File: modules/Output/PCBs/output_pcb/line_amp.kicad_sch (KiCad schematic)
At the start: 23 parts, among them U7 TL074, U8 NE5532, U9 NE5532

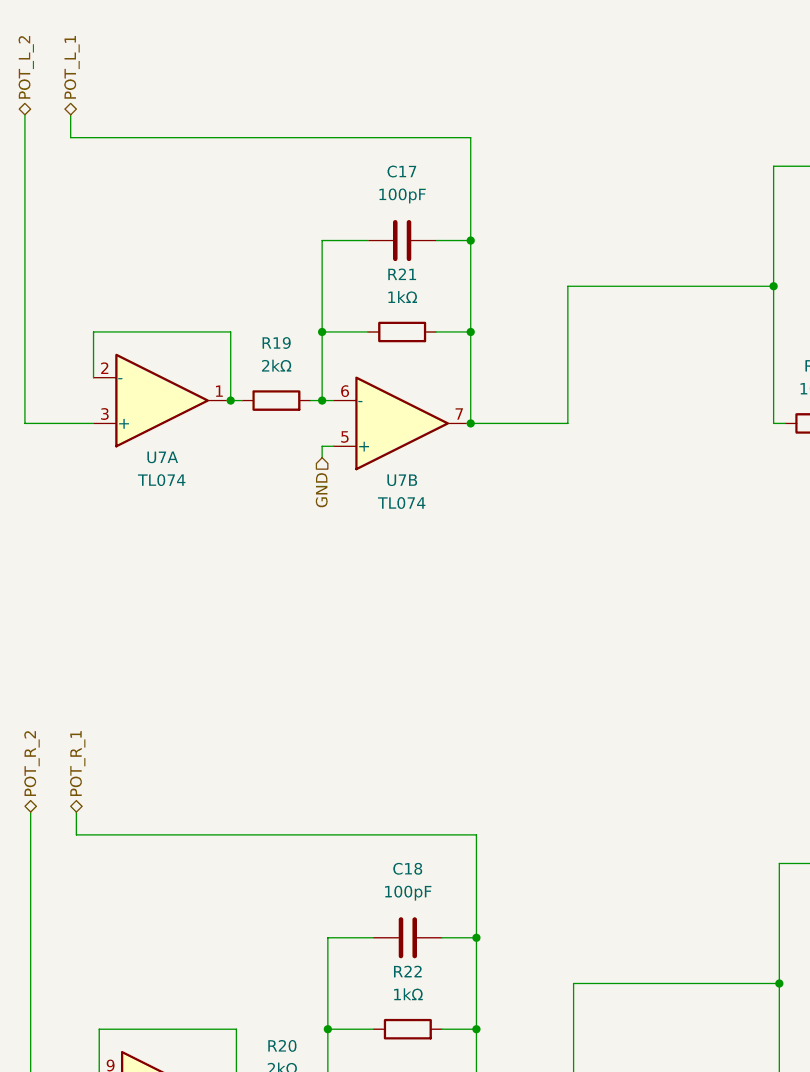
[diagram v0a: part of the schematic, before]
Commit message: finish output PCB
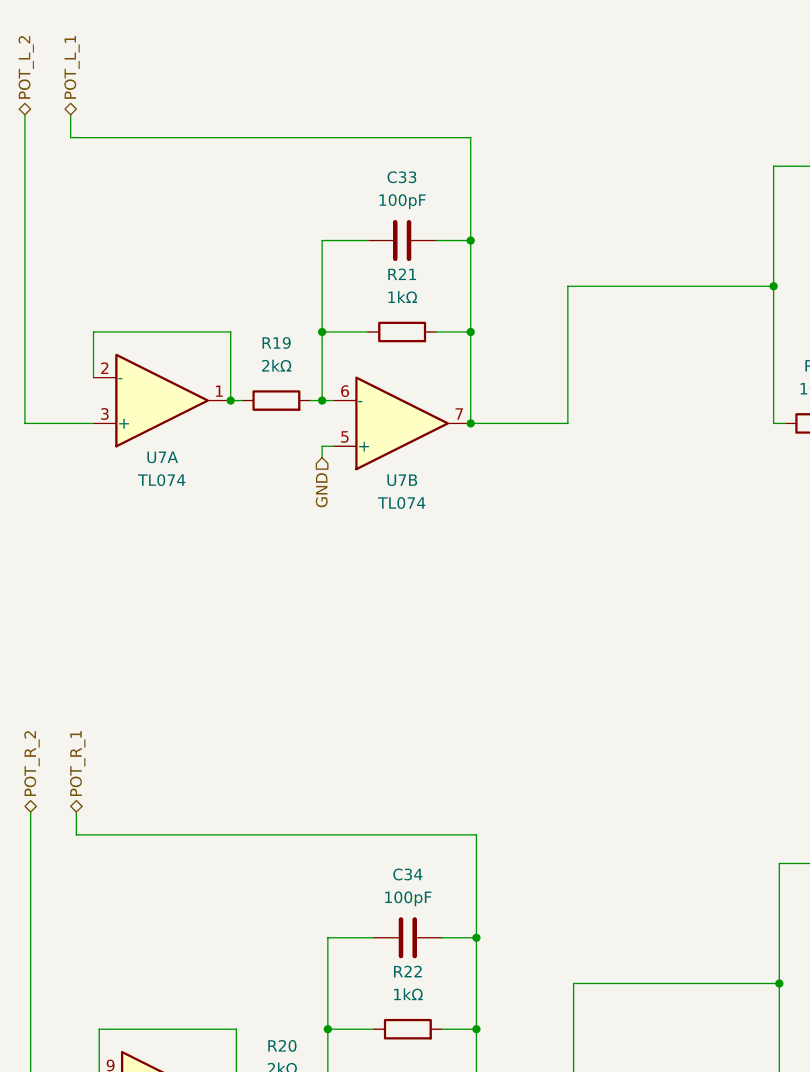
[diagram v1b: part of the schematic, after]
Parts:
- renumbered C17 to C33, C18 to C34
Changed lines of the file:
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@@
   (symbol (lib_id "Device:C") (at 88.265 125.095 90) (unit 1)
     (in_bom yes) (on_board yes) (dnp no) (fields_autoplaced)
-    (property "Reference" "C18" (at 88.265 117.475 90)
+    (property "Reference" "C34" (at 88.265 118.11 90)
       (effects (font (size 1.27 1.27)))
     )
-    (property "Value" "100pF" (at 88.265 120.015 90)
+    (property "Value" "100pF" (at 88.265 120.65 90)
       (effects (font (size 1.27 1.27)))
     )
@@
       (project "output_pcb"
         (path "/9afe4d4d-3155-44ea-9484-068db54e495a/1f69d69c-c7f1-4c71-9890-5c181d5a0d7a"
-          (reference "C18") (unit 1)
+          (reference "C34") (unit 1)
         )
       )
@@
   (symbol (lib_id "Device:C") (at 87.63 47.625 90) (unit 1)
     (in_bom yes) (on_board yes) (dnp no) (fields_autoplaced)
-    (property "Reference" "C17" (at 87.63 40.005 90)
+    (property "Reference" "C33" (at 87.63 40.64 90)
       (effects (font (size 1.27 1.27)))
     )
-    (property "Value" "100pF" (at 87.63 42.545 90)
+    (property "Value" "100pF" (at 87.63 43.18 90)
       (effects (font (size 1.27 1.27)))
     )
@@
       (project "output_pcb"
         (path "/9afe4d4d-3155-44ea-9484-068db54e495a/1f69d69c-c7f1-4c71-9890-5c181d5a0d7a"
-          (reference "C17") (unit 1)
+          (reference "C33") (unit 1)
         )
       )

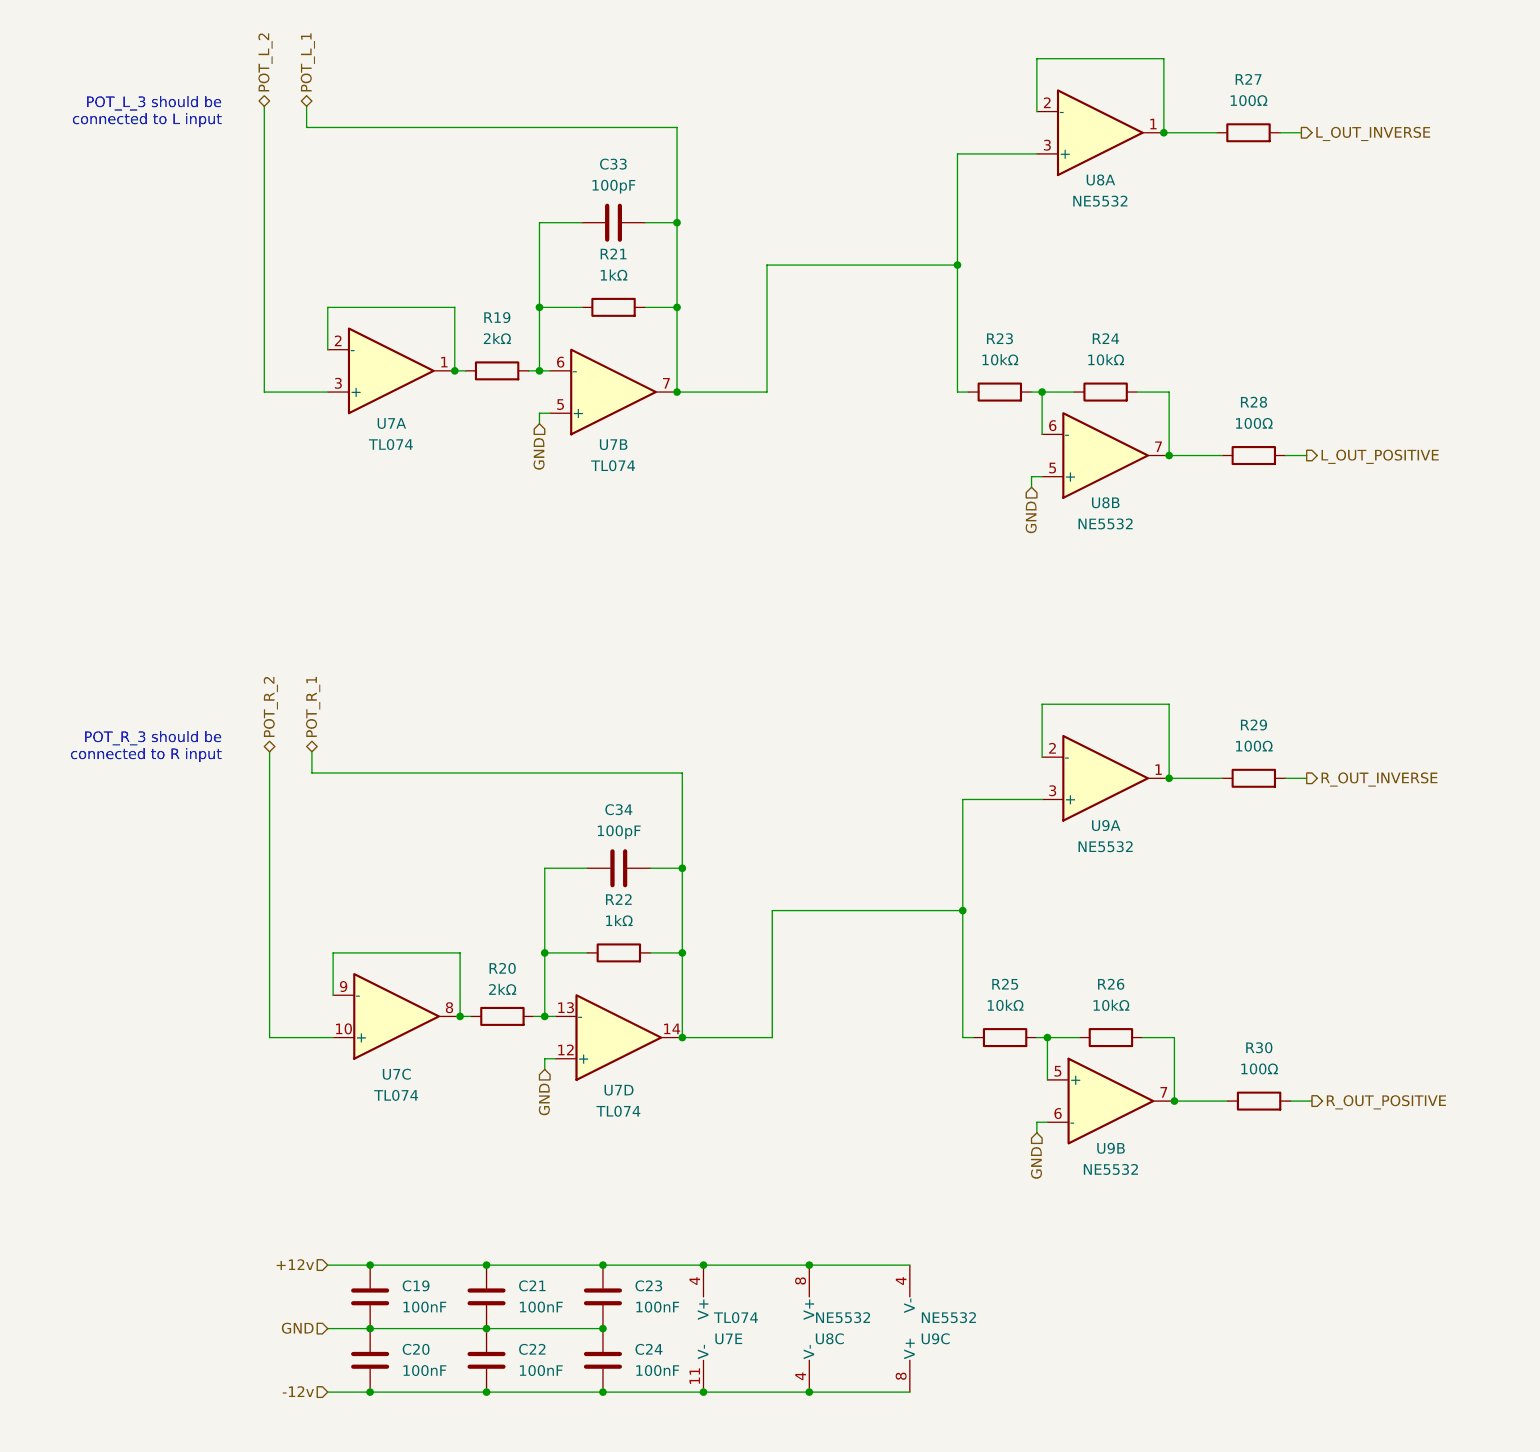
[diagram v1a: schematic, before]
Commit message: fix polarity mismatch bugs in output pcb
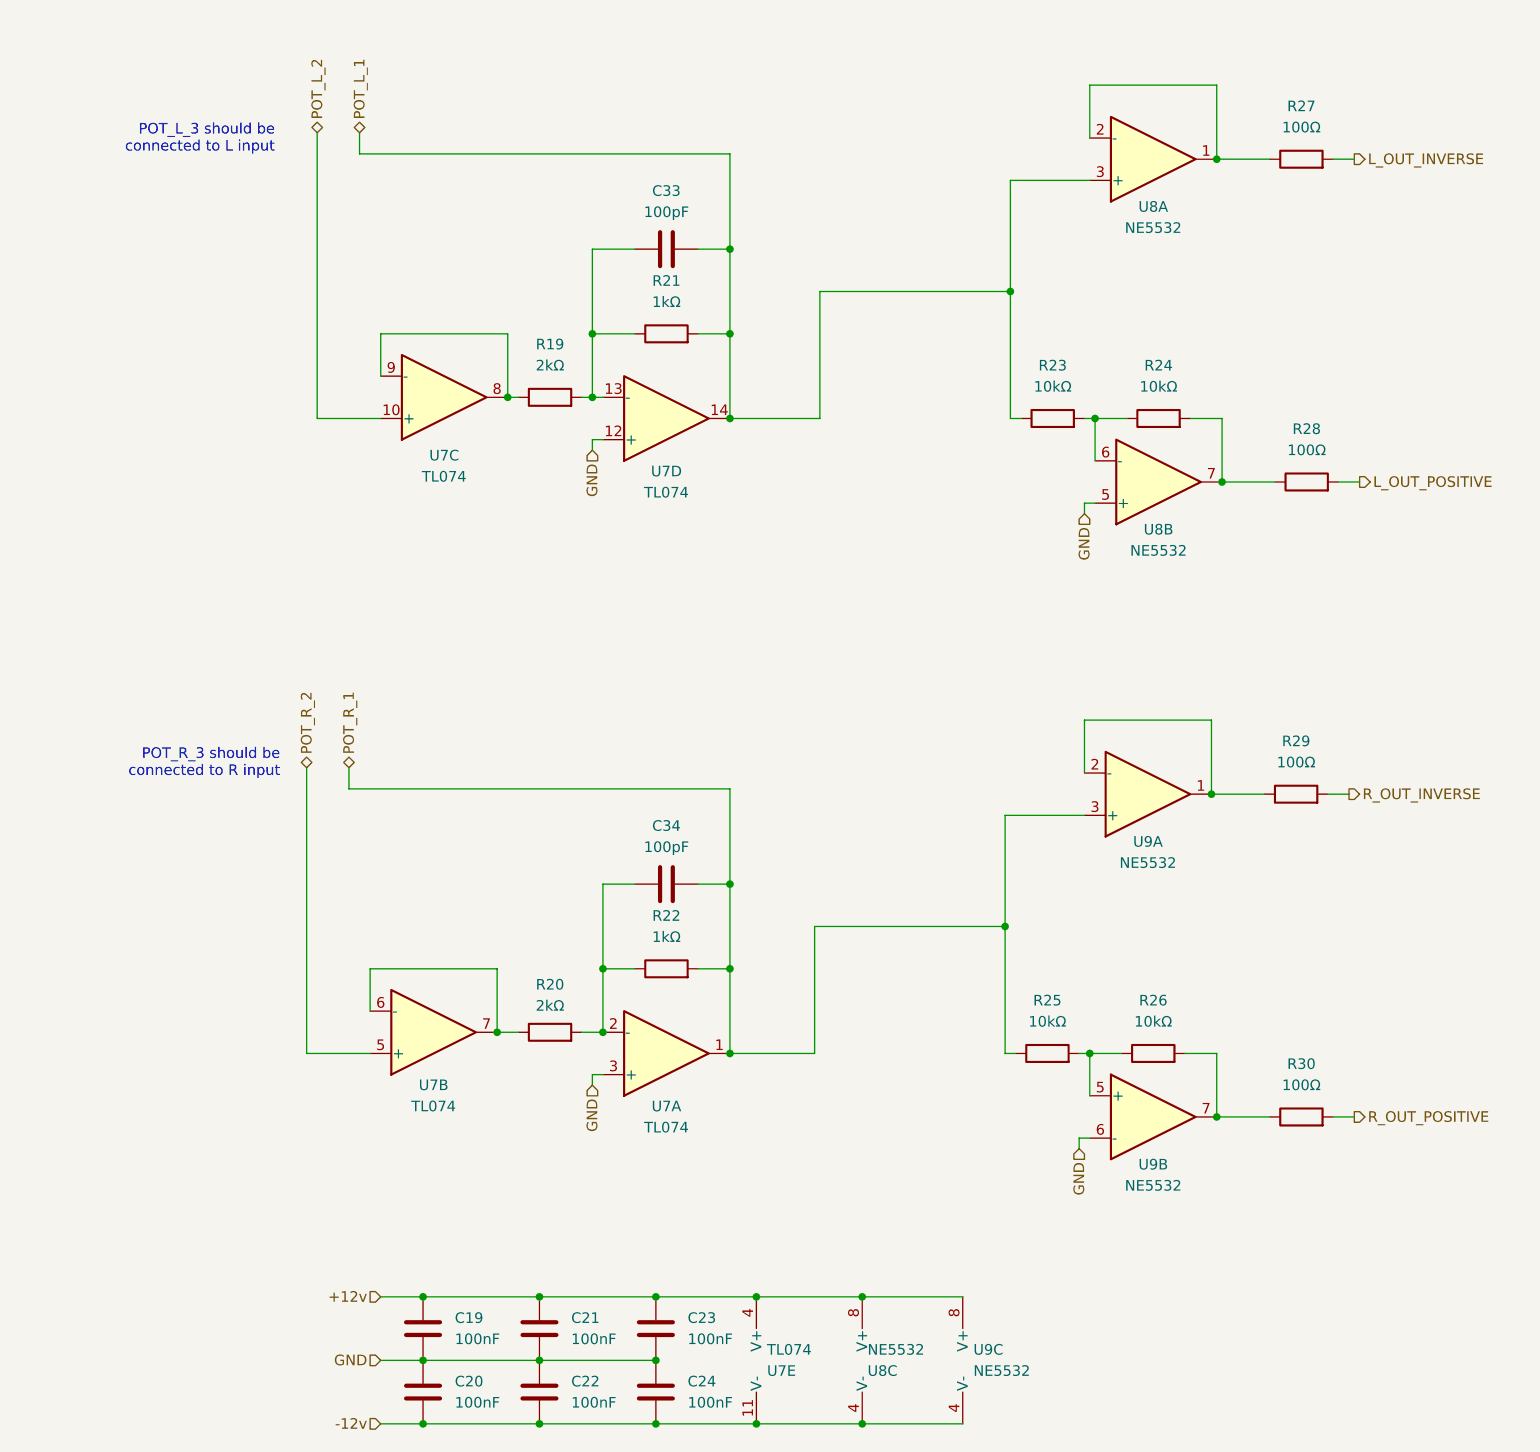
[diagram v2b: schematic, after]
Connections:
- net +12v: now also U9.8 (V+); no longer U9.4 (V-)
- net -12v: now also U9.4 (V-); no longer U9.8 (V+)
- net GND: now also U7.3 (+); no longer U7.5 (+)
- net POT_L_1: now also U7.14; no longer U7.7
- net POT_L_2: now also U7.10 (+); no longer U7.3 (+)
- net POT_R_1: now also U7.1; no longer U7.14
- net POT_R_2: now also U7.5 (+); no longer U7.10 (+)
- net at C34.1, R20.2, R22.1: now also U7.2 (-); no longer U7.13 (-)
- net at U7.8, U7.9 (-): now also R19.1; no longer R20.1
- net at C33.1, R19.2, R21.1: now also U7.13 (-); no longer U7.6 (-)
- new net: R20.1, U7.6 (-), U7.7
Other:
- company: (none) -> Free Modular
- title: (none) -> Output
- moved on the sheet: C19, C20, C21, C22, C23, C24, C33, C34, R19, R20, R21, R22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

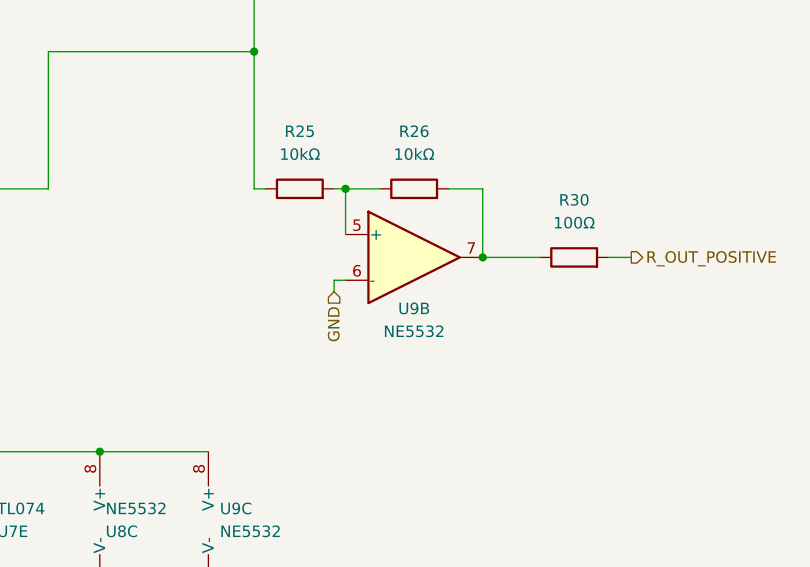
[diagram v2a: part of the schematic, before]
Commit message: Fix errors in output PCB
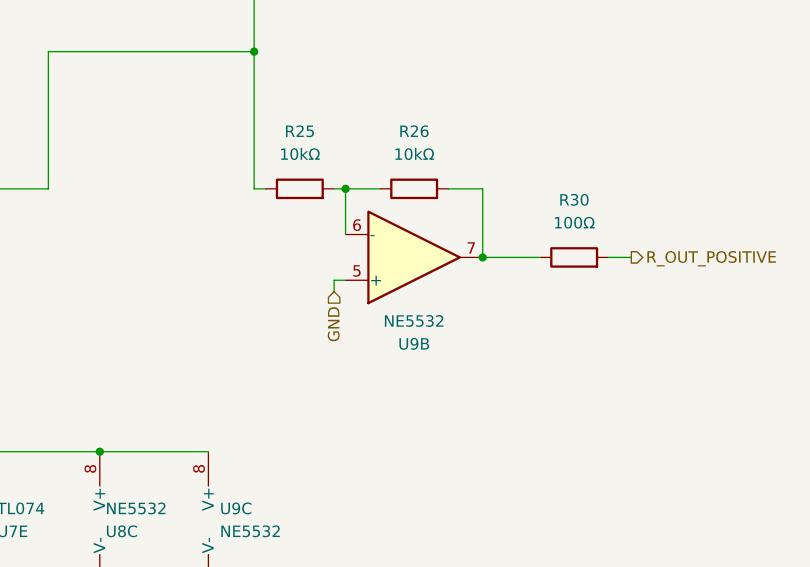
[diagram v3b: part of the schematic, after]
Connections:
- net GND: now also U9.5 (+); no longer U9.6 (-)
- net at R25.2, R26.1: now also U9.6 (-); no longer U9.5 (+)
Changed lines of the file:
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@@
 		(lib_id "Amplifier_Operational:NE5532")
 		(at 152.4 154.94 0)
+		(mirror x)
 		(unit 2)
 		(exclude_from_sim no)
@@
 		(dnp no)
 		(property "Reference" "U9"
-			(at 152.4 160.655 0)
+			(at 152.4 164.592 0)
 			(effects
 				(font
@@
 		)
 		(property "Value" "NE5532"
-			(at 152.4 163.195 0)
+			(at 152.4 162.052 0)
 			(effects
 				(font

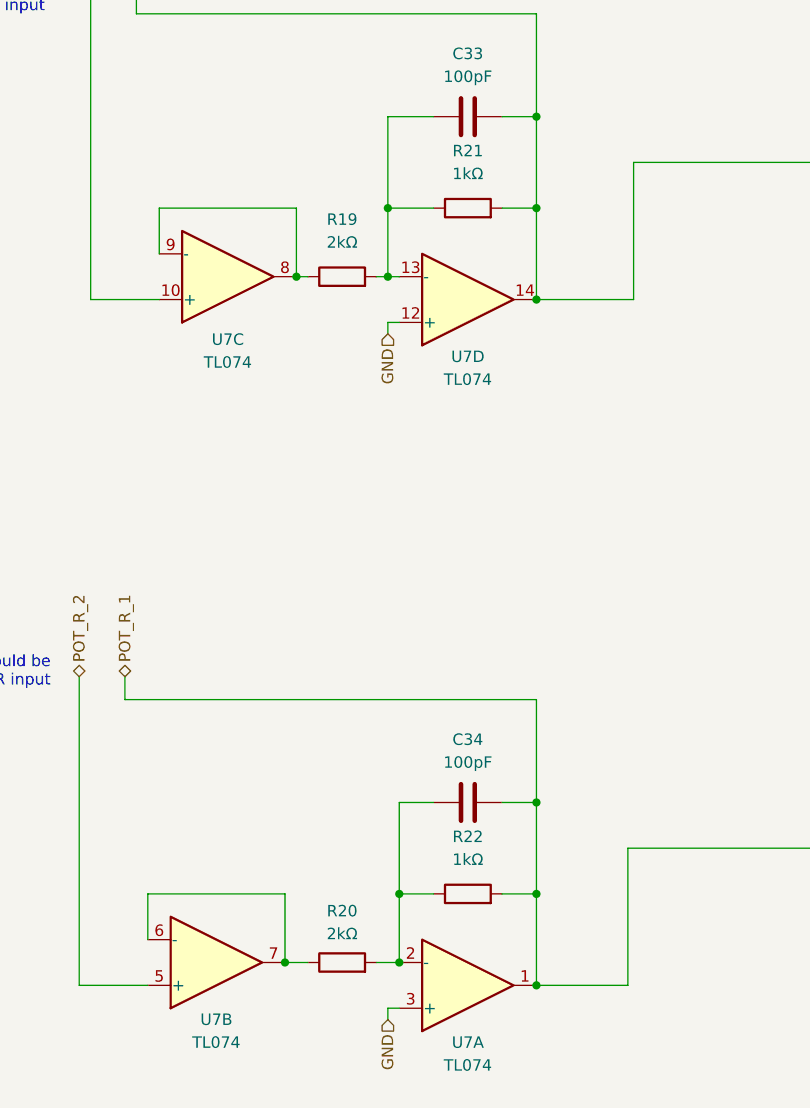
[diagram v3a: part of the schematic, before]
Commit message: Update resistor values in output amp
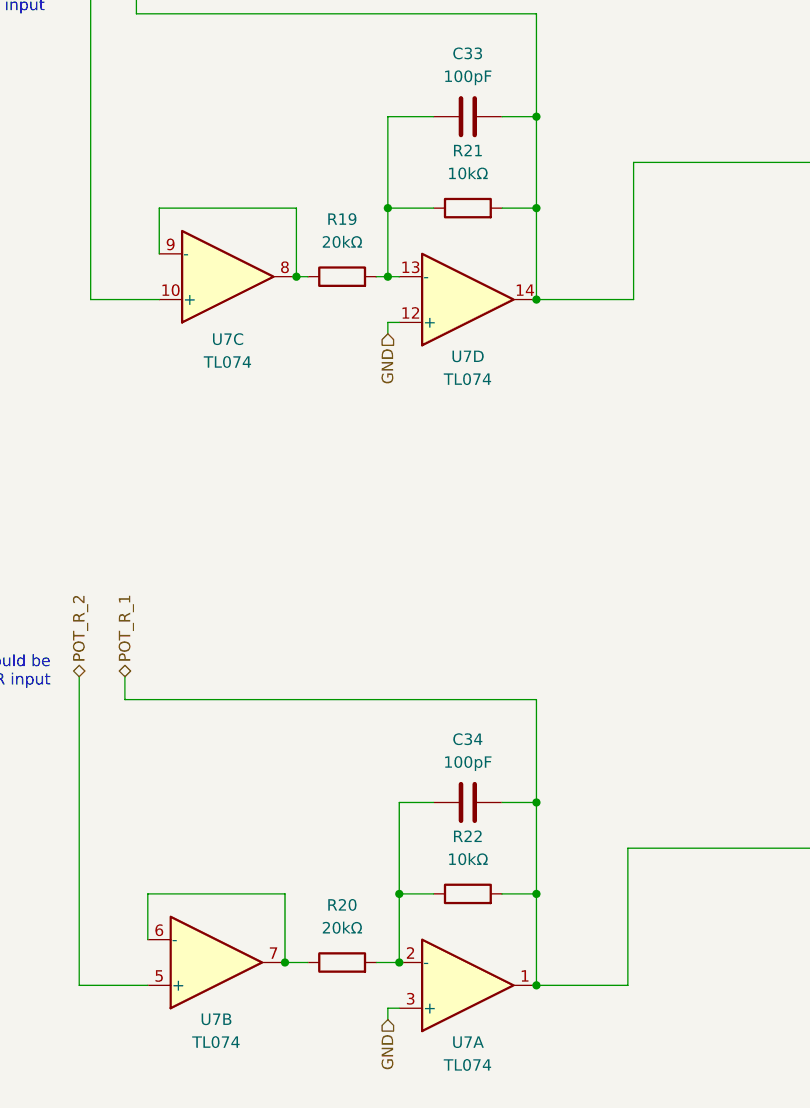
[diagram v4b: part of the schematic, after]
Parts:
- R19, R20: value 2kΩ -> 20kΩ
- R21, R22: value 1kΩ -> 10kΩ
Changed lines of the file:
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@@
 			)
 		)
-		(property "Value" "1kΩ"
+		(property "Value" "10kΩ"
 			(at 93.98 133.35 90)
 			(effects
@@
 			)
 		)
-		(property "Value" "2kΩ"
+		(property "Value" "20kΩ"
 			(at 80.01 64.77 90)
 			(effects
@@
 			)
 		)
-		(property "Value" "1kΩ"
+		(property "Value" "10kΩ"
 			(at 93.98 57.15 90)
 			(effects
@@
 		(fields_autoplaced yes)
 		(property "Reference" "R20"
-			(at 80.01 139.065 90)
-			(effects
-				(font
-					(size 1.27 1.27)
-				)
-			)
-		)
-		(property "Value" "2kΩ"
-			(at 80.01 141.605 90)
-			(effects
-				(font
+			(at 80.01 138.43 90)
+			(effects
+				(font
+					(size 1.27 1.27)
+				)
+			)
+		)
+		(property "Value" "20kΩ"
+			(at 80.01 140.97 90)
+			(effects
+				(font
